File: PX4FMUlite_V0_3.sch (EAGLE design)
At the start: 154 parts, among them J2 DF13-4P-1.25V, J201 DF13C-6P-1.25V, J202 DF13C-6P-1.25V, J203 DF13C-6P-1.25V, J3 DF13C-4P-1.25V, J302 DF13C-4P-1.25V, J401 DF13C-4P-1.25V, J403 DF13C-7P-1.25V, J405 DF13C-4P-1.25V, J801 JST-ZH-3, J802 DF13C-3P-1.25V, M3_MOUNT1101 MOUNT-HOLE3.1MM, M3_MOUNT1102 MOUNT-HOLE3.1MM, M3_MOUNT1103 MOUNT-HOLE3.1MM, M3_MOUNT1104 MOUNT-HOLE3.1MM, U101 STM32F4X7VX, U2 MAX3051, U401 MAX3051, U903 74LVC2G240, X101 3.2x2.5 mm / 24 MHz / 15 ppm

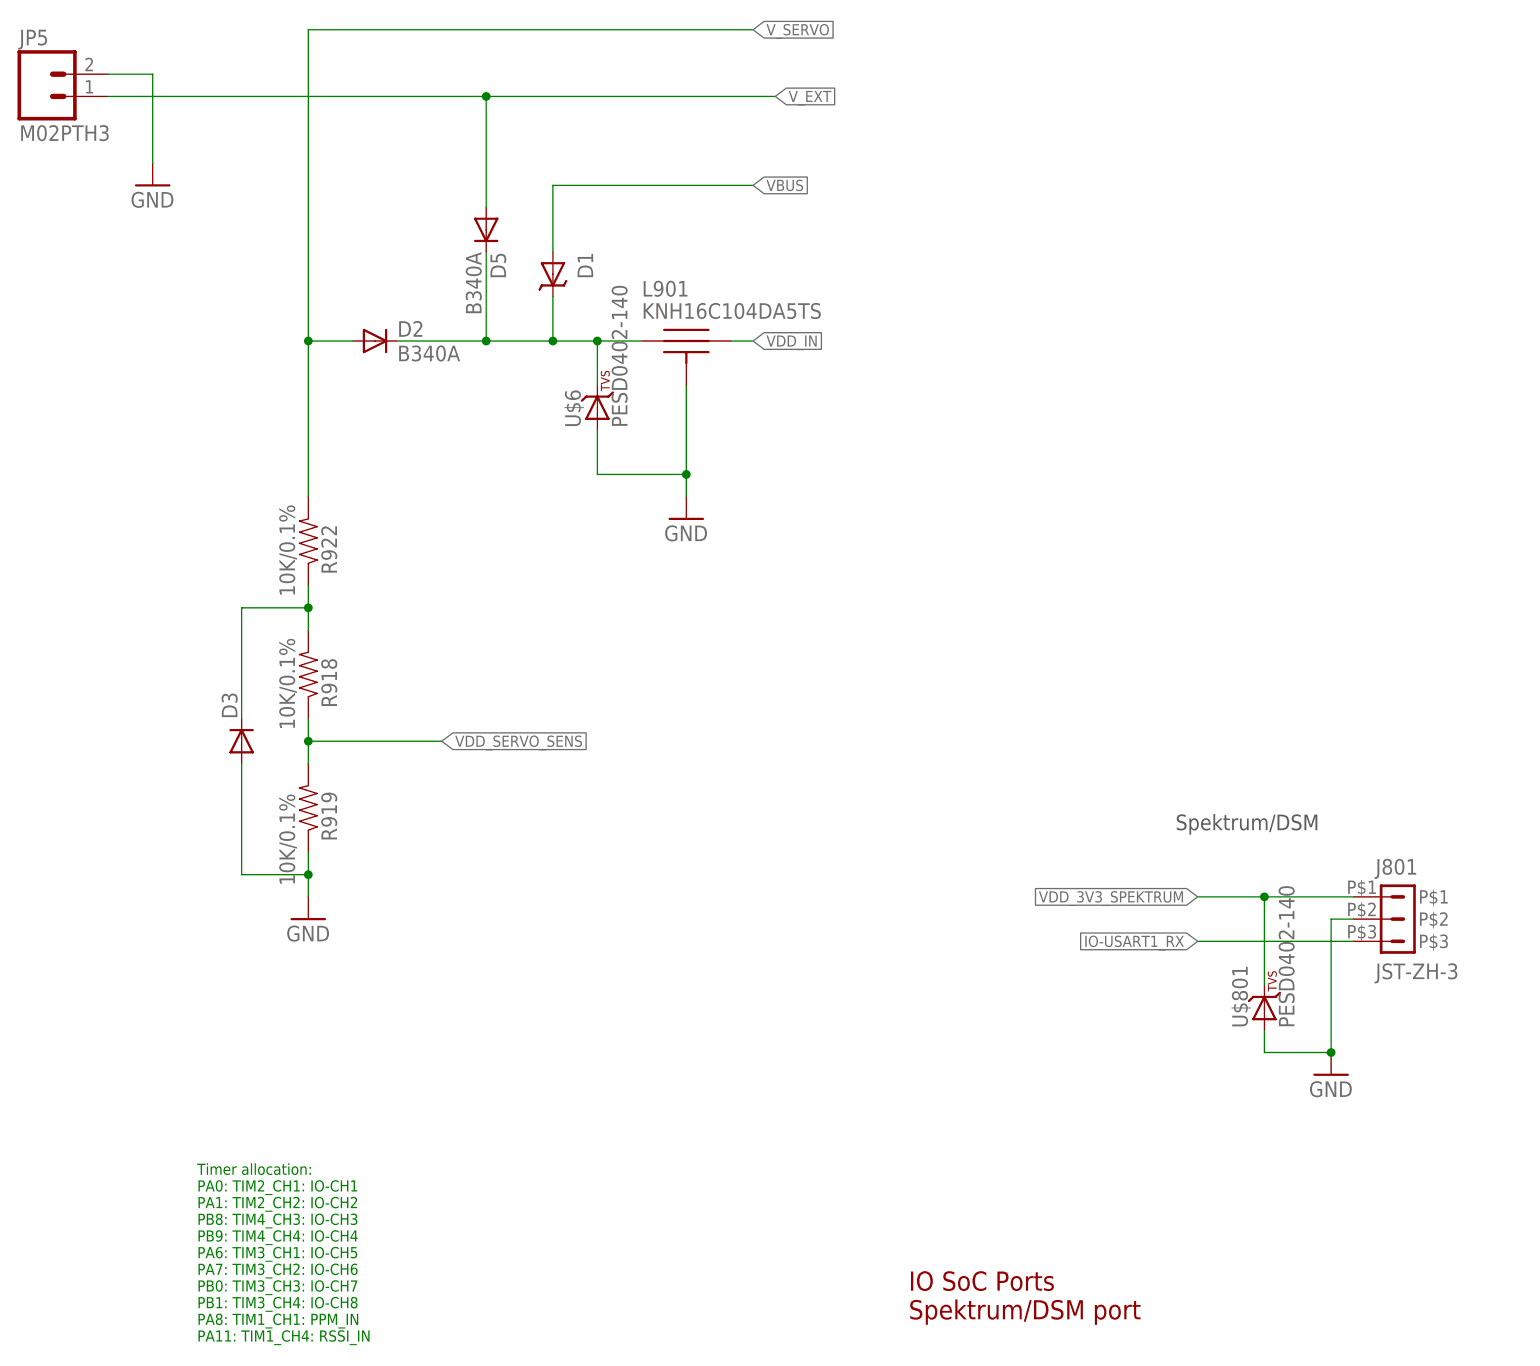
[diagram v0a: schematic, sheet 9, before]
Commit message: Filter taken from Vin since it is well decoupled through TPS63031
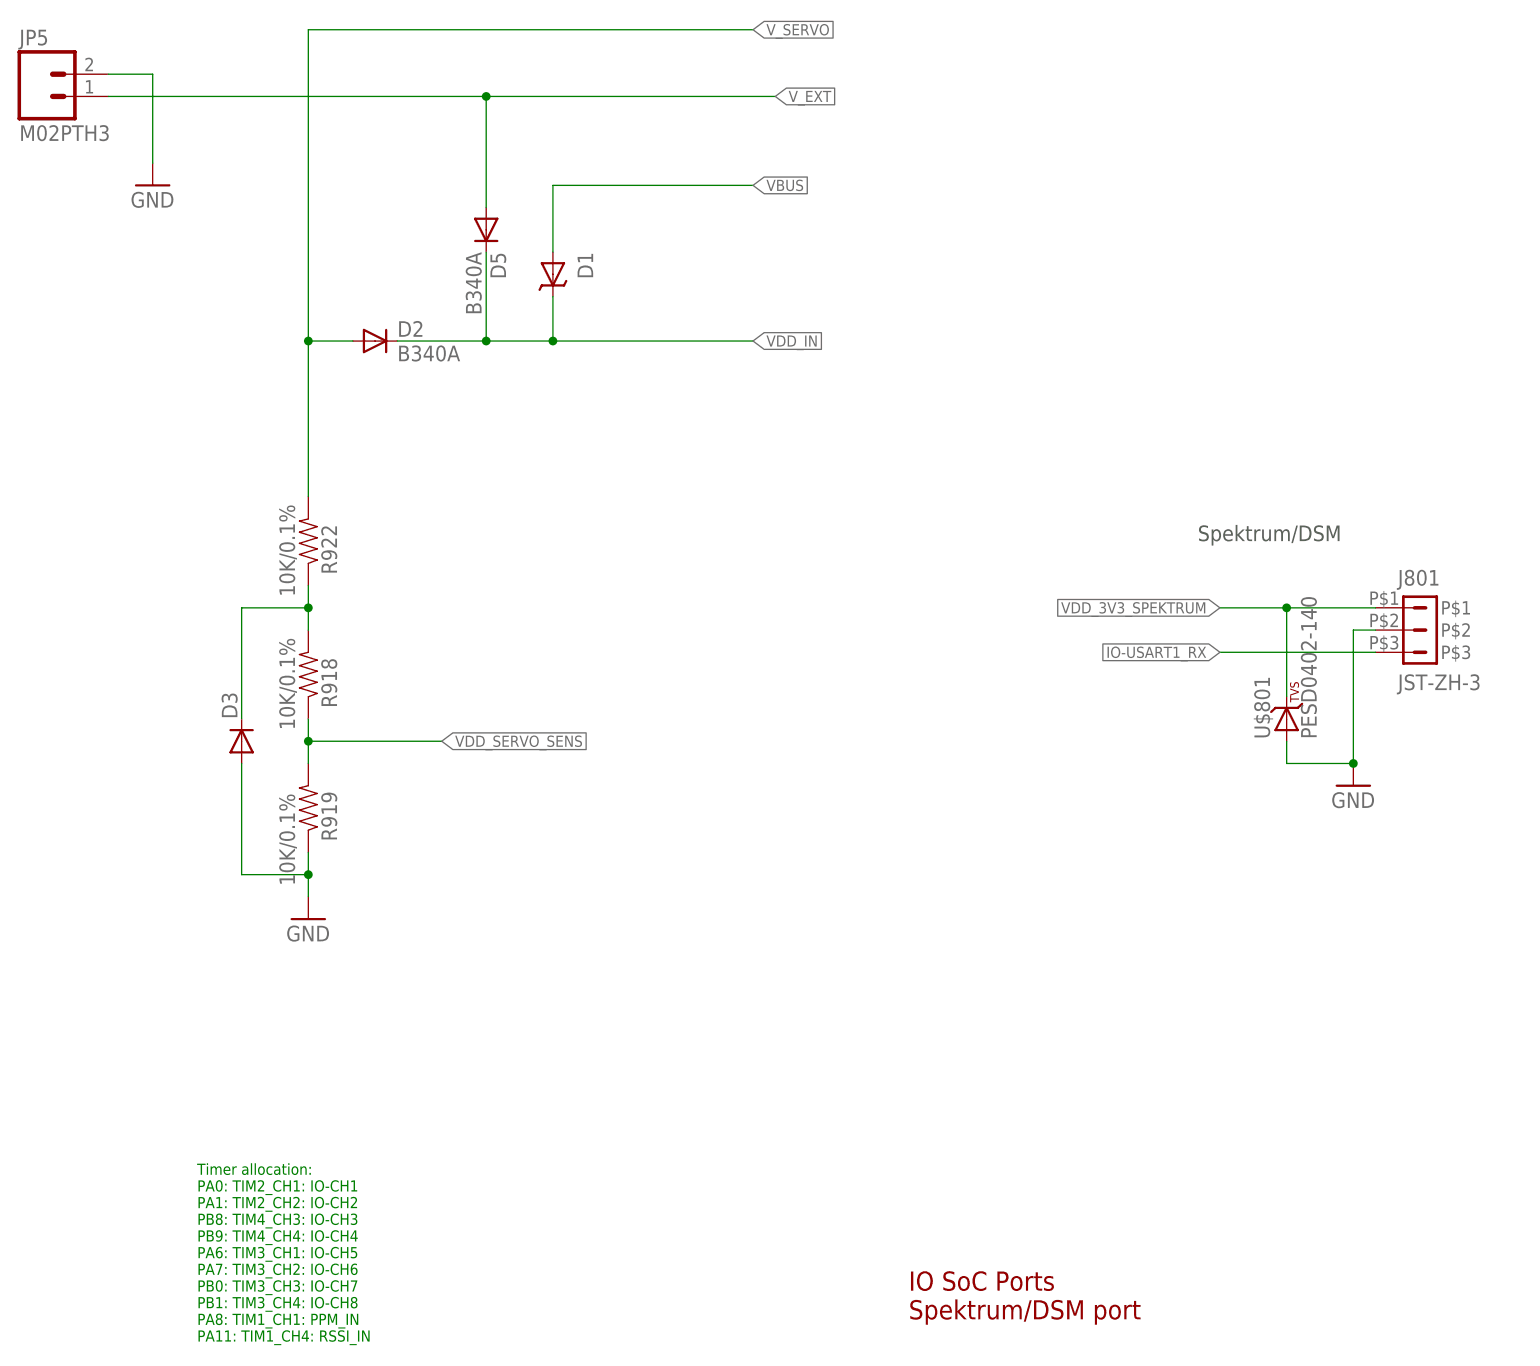
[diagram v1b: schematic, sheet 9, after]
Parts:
- removed L901: KNH16C104DA5TS, pixhawk2:KNH16C104DA5TS
- removed U$6: PESD0402-140, pixhawk2:DIODE-TVS
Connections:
- removed net V_OR_D: D1.C, D2.C, D5.C, L901.P$1, U$6.C
- net FMU-I2C1_SCL: now also L6G$8.P$1; no longer L6G$3.P$1
- net FMU-I2C1_SDA: now also L6G$7.P$1; no longer L6G$4.P$1
- net FMU-I2C2_SCL: now also L6G$2.P$1; no longer L6G$1.P$1
- net FMU-I2C2_SDA: now also L6G$1.P$1; no longer L6G$2.P$1
- net GND: no longer L901.P$3, U$6.A
- net N$20: now also L6G$1.P$2; no longer L6G$2.P$2
- net N$33: now also L6G$8.P$2; no longer L6G$3.P$2
- net N$37: now also L6G$7.P$2; no longer L6G$4.P$2
- net N$4: now also L6G$2.P$2; no longer L6G$1.P$2
- net VDD_IN: now also D1.C, D2.C, D5.C; no longer L901.P$2
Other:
- moved on the sheet: J801, L6G$1, L6G$2, L6G$3, L6G$4, L6G$7, L6G$8, U$801
